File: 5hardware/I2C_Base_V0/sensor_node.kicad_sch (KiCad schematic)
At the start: 66 parts, among them J2 PJ-320D-A, J3 Conn_02x06_Top_Bottom, J4 Conn_01x19_Socket, J5 Conn_01x19_Socket, J6 Conn_01x06_Socket, J7 Conn_01x04_Pin, J8 Conn_01x04_Pin, P1 S3B-PH-SM4-TB, P2 S4B-PH-SM4-TB, P3 S3B-PH-SM4-TB, Q2 Si2371EDS, Q3 Si2371EDS, SW2 SW_Push, SW3 SW_Push, U10 ESP-12F, U12 APDS-9960, U14 DS3231M, U3 CR2450, U4 CH32V003F4P6, U5 SHT31-DIS, U6 DS1307Z+, U7 XC6206PxxxMR, U8 TPL5110, U9 BH1750FVI-TR, Y1 Crystal, Y2 Crystal

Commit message: update PCB.
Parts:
- removed C1, C3, C5, C6: C, Capacitor_SMD:C_1206_3216Metric, symbol Device:C
- removed D1, D10, D3, D4, D5: LED, LED_SMD:LED_0603_1608Metric, symbol Device:LED
- removed J3: Conn_02x06_Top_Bottom, Connector_PinHeader_2.54mm:PinHeader_2x06_P2.54mm_Vertical, symbol Connector_Generic:Conn_02x06_Top_Bottom
- removed J4, J5: Conn_01x19_Socket, Connector_PinSocket_2.54mm:PinSocket_1x19_P2.54mm_Vertical, symbol Connector:Conn_01x19_Socket
- removed J6: Conn_01x06_Socket, Connector_PinHeader_2.00mm:PinHeader_1x06_P2.00mm_Vertical, symbol Connector:Conn_01x06_Socket
- removed J7, J8: Conn_01x04_Pin, Connector_PinHeader_1.27mm:PinHeader_1x04_P1.27mm_Vertical, symbol Connector:Conn_01x04_Pin
- removed P2: S4B-PH-SM4-TB, S4B-PH:JST_S4B-PH-SM4-TB, symbol JST_S4B-PH:S4B-PH-SM4-TB
- removed R1, R16, R17, R18, R19, R22: R, Resistor_SMD:R_0603_1608Metric, symbol Device:R
- removed R10, R28, R8: R, Resistor_SMD:R_0805_2012Metric, symbol Device:R
- removed R25, R26, R27: R, Resistor_SMD:R_1206_3216Metric, symbol Device:R
- removed SW2: SW_Push, Button_Switch_SMD:SW_SPST_PTS810, symbol Switch:SW_Push
- removed U10: ESP-12F, A_SensorNode:ESP12_SMD, symbol ESP8266:ESP-12F
- removed U11: ~, A_SensorNode:JDY-Base, symbol A_SensorNode:JDY-Base
- removed U12: APDS-9960, Sensor:Avago_APDS-9960, symbol Sensor:APDS-9960
- removed U14: DS3231M, Package_SO:SOIC-16W_7.5x10.3mm_P1.27mm, symbol Timer_RTC:DS3231M
- removed U2: ~, A_SensorNode:E104-BT07, symbol A_SensorNode:E104-BT07
- removed U5: SHT31-DIS, Sensor_Humidity:Sensirion_DFN-8-1EP_2.5x2.5mm_P0.5mm_EP1.1x1.7mm, symbol Sensor_Humidity:SHT31-DIS
- removed U6: DS1307Z+, Package_SO:SOIC-8_3.9x4.9mm_P1.27mm, symbol Timer_RTC:DS1307Z+
- removed U9: BH1750FVI-TR, BH1750:XDCR_BH1750FVI-TR, symbol BH1750FVI-TR:BH1750FVI-TR
- removed Y1: Crystal, Crystal:Crystal_SMD_3215-2Pin_3.2x1.5mm, symbol Device:Crystal
- removed Y2: Crystal, Crystal:Crystal_Round_D1.5mm_Vertical, symbol Device:Crystal
- added C10, C9: C, Capacitor_SMD:C_0805_2012Metric, symbol Device:C
- added J3: USB_C_Receptacle_USB2.0, Connector_USB:USB_C_Receptacle_G-Switch_GT-USB-7010ASV, symbol Connector:USB_C_Receptacle_USB2.0
- added J5: Conn_01x15_Pin, Connector_PinHeader_2.54mm:PinHeader_1x15_P2.54mm_Vertical, symbol Connector:Conn_01x15_Pin
- added Q1: Si2371EDS, Package_TO_SOT_SMD:SOT-23, symbol Transistor_FET:Si2371EDS
- added Q5: MMBT5551L, Package_TO_SOT_SMD:SOT-23, symbol Transistor_BJT:MMBT5551L
- added R31, R32, R33, R34: R, Resistor_SMD:R_0603_1608Metric, symbol Device:R
- added R35, R40, R41, R42, R43: R, Resistor_SMD:R_0805_2012Metric, symbol Device:R
- added U6: MCP1700x-330xxTO, Package_TO_SOT_THT:TO-92_Inline, symbol Regulator_Linear:MCP1700x-330xxTO
- C2: footprint Capacitor_SMD:C_1206_3216Metric -> Capacitor_SMD:C_0805_2012Metric
- R14, R15, R2, R3: footprint Resistor_SMD:R_1206_3216Metric -> Resistor_SMD:R_0805_2012Metric
- R23: footprint Resistor_SMD:R_0603_1608Metric -> Resistor_SMD:R_0805_2012Metric
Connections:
- net Vin- is gone; now on net GND: R23.2
- net +3.3V: now also C9.1, J5.14 (Pin_14), U6.3 (VO)
- net +5V: now also C10.1, J3.A4 (VBUS), J3.A9 (VBUS), J3.B4 (VBUS), J3.B9 (VBUS), Q1.2 (S), R43.1
- net Bat-Vi: now also J5.1 (Pin_1), R33.2
- net Bat-Vo: now also J5.2 (Pin_2), R31.2
- net D+: now also J3.A6 (D+), J3.B6 (D+)
- net D-: now also J3.A7 (D-), J3.B7 (D-)
- net DONE: now also J5.8 (Pin_8)
- net DRV: now also J5.9 (Pin_9)
- net GND: now also C10.2, C9.2, J3.A1 (GND), J3.A12 (GND), J3.B1 (GND), J3.B12 (GND), J3.S1 (SHIELD), J5.15 (Pin_15), Q5.2 (E), R35.2, R41.1, U6.1 (GND)
- net PD2: now also R40.1, R41.2
- net Solar_Vi: now also J5.5 (Pin_5), R34.1
- net Solar_Vo: now also J5.6 (Pin_6), R32.1; no longer R23.1
- net Vo: now also J5.7 (Pin_7), U6.2 (VI)
- net at R15.1: now also D6.3; no longer D6.1
- net at R7.2: now also D6.1
- net at D6.4, R14.1: no longer D6.3
- net MISO renamed ROTB
- net MOSI renamed ROTA
- net RX renamed RX1
- net SCK: no longer names the net of U4.15 (PC5)
- net SCK: now also R42.2
- net SCL (5) renamed SCL0
- net SCL0: now also J5.13 (Pin_13)
- net SDA (4) renamed SDA0
- net SDA0: now also J5.12 (Pin_12)
- net TX renamed TX1
- new net: J3.B5 (CC2), R35.1
- new net: Q1.1 (G), Q5.3 (C), R43.2
- new net: Q1.3 (D), R40.2
- new net: Q5.1 (B), R42.1
- new net: J3.A5 (CC1), R23.1
- new net CS0: J5.10 (Pin_10)
- new net CS1: J5.11 (Pin_11)
- new net Vi+: J5.3 (Pin_3), R33.1, R34.2
- new net Vi-: J5.4 (Pin_4), R31.1, R32.2
- no-connect marks 49 -> 5
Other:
- added sheet ESP12 (ESP12.kicad_sch)
- moved on the sheet: C2, D2, D6, J2, P1, P3, Q2, Q3, R11, R15, R2, R20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

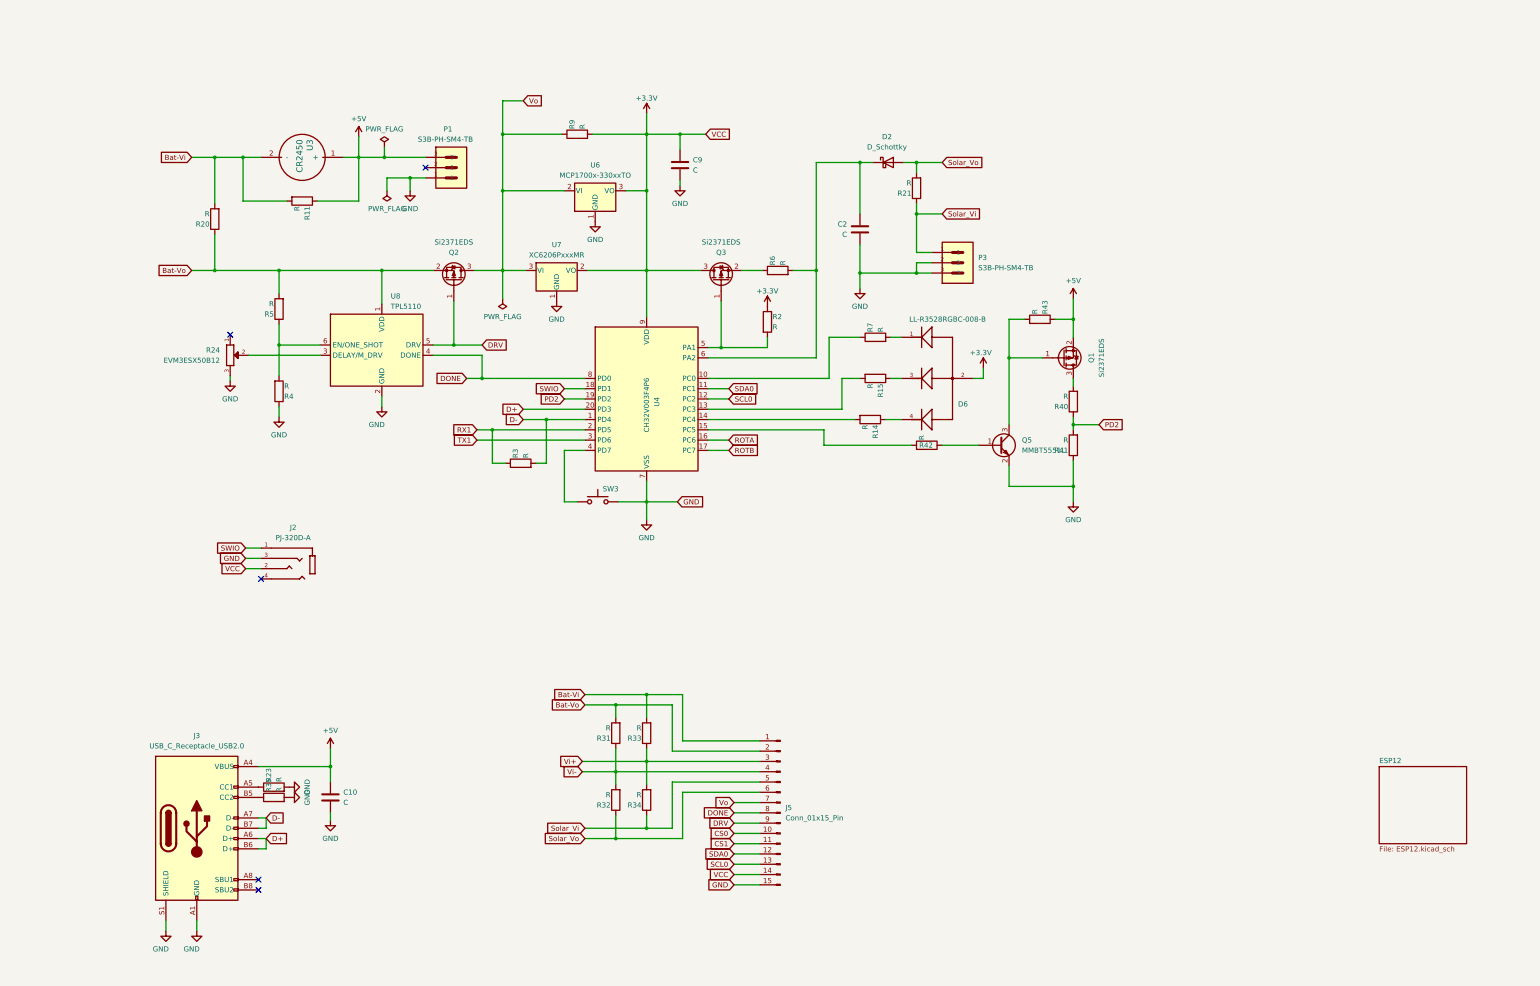
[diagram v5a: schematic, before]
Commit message: update schematic.
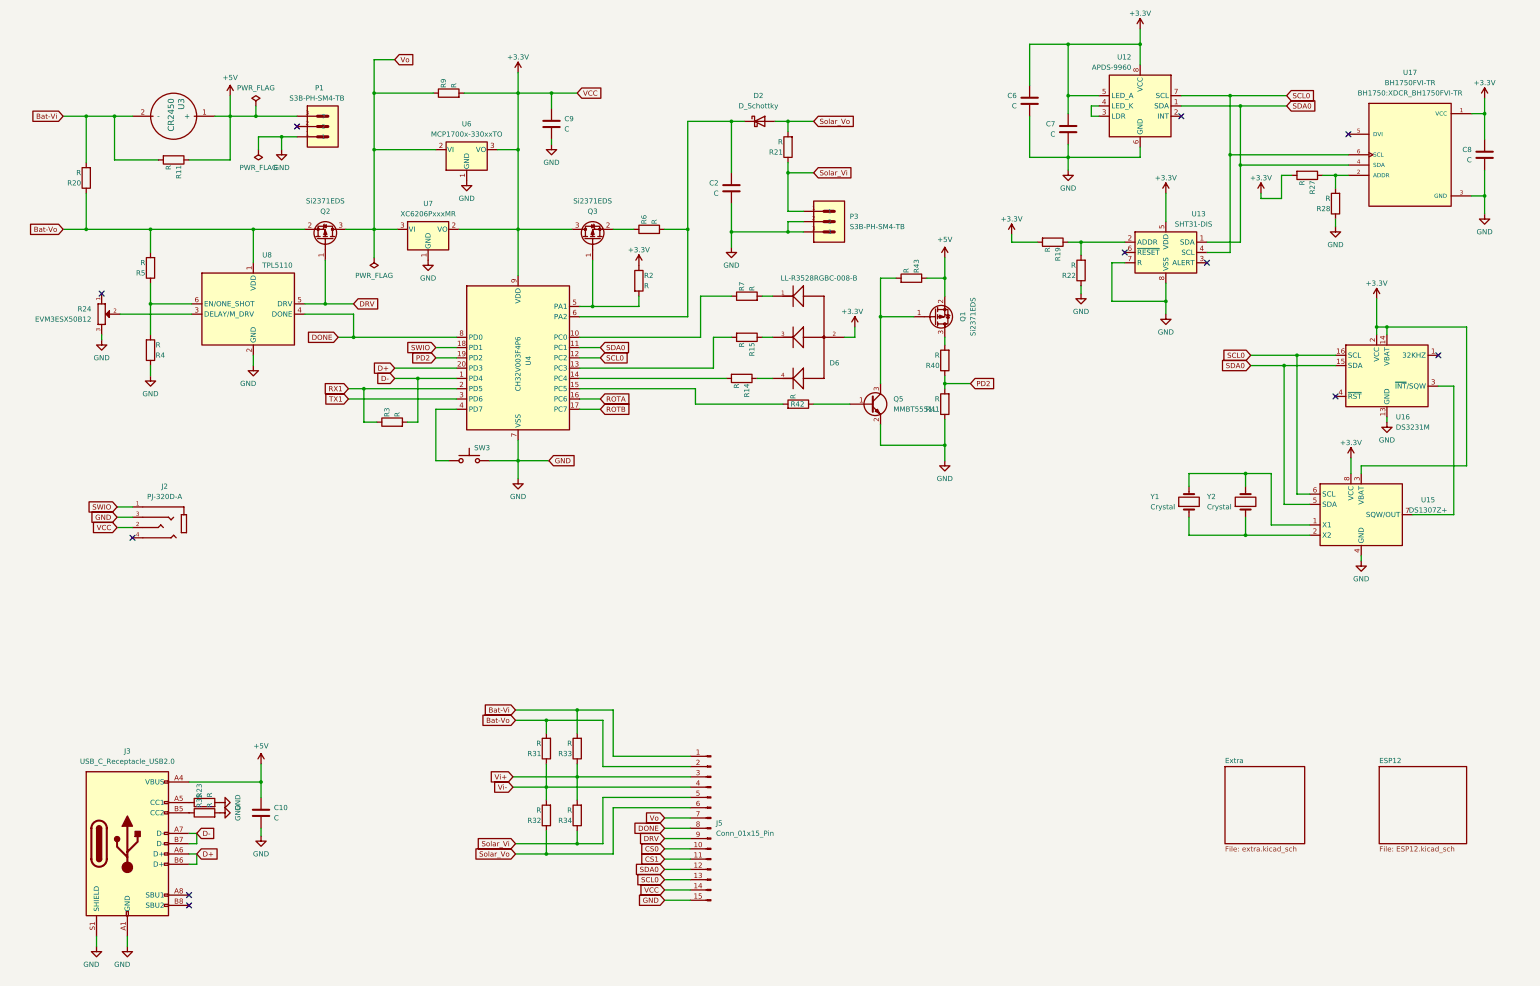
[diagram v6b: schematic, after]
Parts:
- added C6, C7, C8: C, Capacitor_SMD:C_0805_2012Metric, symbol Device:C
- added R19, R22, R27, R28: R, Resistor_SMD:R_0603_1608Metric, symbol Device:R
- added U12: APDS-9960, Sensor:Avago_APDS-9960, symbol Sensor:APDS-9960
- added U13: SHT31-DIS, Sensor_Humidity:Sensirion_DFN-8-1EP_2.5x2.5mm_P0.5mm_EP1.1x1.7mm, symbol Sensor_Humidity:SHT31-DIS
- added U15: DS1307Z+, Package_SO:SOIC-8_3.9x4.9mm_P1.27mm, symbol Timer_RTC:DS1307Z+
- added U16: DS3231M, Package_SO:SOIC-16W_7.5x10.3mm_P1.27mm, symbol Timer_RTC:DS3231M
- added U17: BH1750FVI-TR, BH1750:XDCR_BH1750FVI-TR, symbol BH1750FVI-TR:BH1750FVI-TR
- added Y1: Crystal, Crystal:Crystal_Round_D1.5mm_Vertical, symbol Device:Crystal
- added Y2: Crystal, Crystal:Crystal_SMD_3215-2Pin_3.2x1.5mm, symbol Device:Crystal
- J3: footprint Connector_USB:USB_C_Receptacle_G-Switch_GT-USB-7010ASV -> Connector_USB:USB_C_Receptacle_HRO_TYPE-C-31-M-12
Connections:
- net +3.3V: now also C6.1, C7.1, C8.1, R19.2, R27.2, U12.5 (LED_A), U12.8 (VCC), U13.5 (VDD), U15.3 (VBAT), U15.8 (VCC), U16.14 (VBAT), U16.2 (VCC), U17.1 (VCC)
- net GND: now also C6.2, C7.2, C8.2, R22.1, R28.1, U12.6 (GND), U13.7 (R), U13.8 (VSS), U13.9 (VSS), U15.4 (GND), U16.10 (GND), U16.11 (GND), U16.12 (GND), U16.13 (GND), U16.5 (GND), U16.6 (GND), U16.7 (GND), U16.8 (GND), U16.9 (GND), U17.3 (GND)
- net SCL0: now also U12.7 (SCL), U13.4 (SCL), U15.6 (SCL), U16.16 (SCL), U17.6 (SCL)
- net SDA0: now also U12.1 (SDA), U13.1 (SDA), U15.5 (SDA), U16.15 (SDA), U17.4 (SDA)
- new net: U15.2 (X2), Y1.1, Y2.1
- new net: U15.1 (X1), Y1.2, Y2.2
- new net: R27.1, R28.2, U17.2 (ADDR)
- new net: U12.3 (LDR), U12.4 (LED_K)
- new net: U15.7 (SQW/OUT), U16.3 (~{INT}/SQW)
- new net: R19.1, R22.2, U13.2 (ADDR)
- no-connect marks 5 -> 11
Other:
- added sheet Extra (extra.kicad_sch)
- moved on the sheet: C10, C2, C9, D2, D6, J2, J3, J5, P1, P3, Q1, Q2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

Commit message: update PCB.
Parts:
- added J6: Conn_01x07_Pin, Connector_PinSocket_2.00mm:PinSocket_1x07_P2.00mm_Vertical, symbol Connector:Conn_01x07_Pin
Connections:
- net +3.3V: now also J6.1 (Pin_1)
- net +5V: now also J6.7 (Pin_7)
- net GND: now also J6.2 (Pin_2)
- net RX1: now also J6.5 (Pin_5)
- net SCL0: now also J6.3 (Pin_3)
- net SDA0: now also J6.4 (Pin_4)
- net TX1: now also J6.6 (Pin_6)
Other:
- removed sheet Extra
- moved on the sheet: C10, C2, C9, D2, D6, J2, J3, J5, P1, P3, Q1, Q2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
